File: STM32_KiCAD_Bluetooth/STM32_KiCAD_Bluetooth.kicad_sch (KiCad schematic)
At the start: 9 parts, among them U1 STM32WB55CEU6

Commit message: Schematic
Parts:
- removed C7: 1.0uF, SparkFun-Capacitor:C_0603_1608Metric, symbol SparkFun-Capacitor:1.0uF_0603_16V_10%
- removed C8: 10nF, SparkFun-Capacitor:C_0603_1608Metric, symbol SparkFun-Capacitor:1.0uF_0603_16V_10%
- added C10, C8, C9: 0.1uF, SparkFun-Capacitor:C_0603_1608Metric, symbol SparkFun-Capacitor:0.1uF_0603_25V_20%
- added C11, C7: 4.7uF, SparkFun-Capacitor:C_0603_1608Metric, symbol SparkFun-Capacitor:4.7uF_0603_35V_20%
- added L1: 10nH, Inductor_SMD:L_0603_1608Metric, symbol Device:L
- added L2: 10uH, symbol Device:L
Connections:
- net +3.3V: now also U1.23 (VDDRF), U1.34 (VDDSMPS), U1.8 (VDDA), C10.1, C7.1, C8.1, C9.1
- net GND: now also C10.2, C11.2, C7.2, C8.2, C9.2
- net SMPSFB: now reaches U1.31 (VFBSMPS)
- net SMPSFB: now also C11.1, L2.2
- net SMPSLX: now reaches U1.33 (VLXSMPS)
- net SMPSLX: now also L1.1
- new net SMPSLXL: L1.2, L2.1

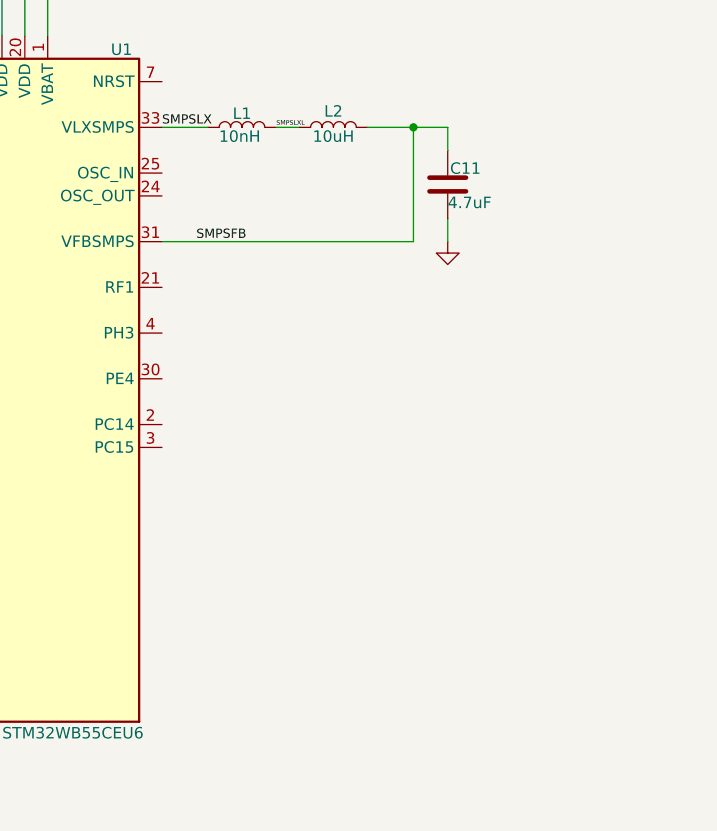
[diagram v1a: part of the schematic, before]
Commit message: Update STM32_KiCAD_Bluetooth.kicad_sch
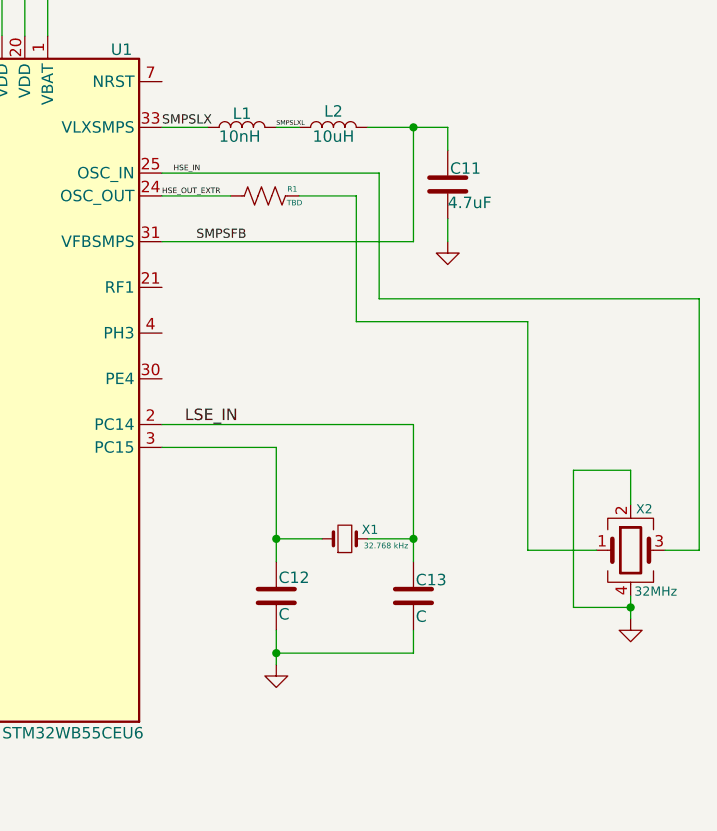
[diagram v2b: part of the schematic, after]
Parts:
- added C12, C13: C, symbol Device:C
- added R1: TBD, SparkFun-Resistor:R_0603_1608Metric, symbol SparkFun-Resistor:330_0603
- added X1: 32.768 kHz, Crystal:Crystal_SMD_2012-2Pin_2.0x1.2mm, symbol SparkFun-Clock:Crystal
- added X2: 32MHz, symbol Device:Crystal_GND24
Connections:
- net GND: now also C12.2, C13.2, X2.2, X2.4
- net LSE_IN: now reaches U1.2 (PC14)
- net LSE_IN: now also C13.1, X1.2
- net HSE_OUT_EXTR: now reaches U1.24 (OSC_OUT)
- net HSE_OUT_EXTR: now also R1.2
- net HSE_IN: now reaches U1.25 (OSC_IN)
- net HSE_IN: now also X2.3
- net at U1.3 (PC15): now also C12.1, X1.1
- new net: R1.1, X2.1

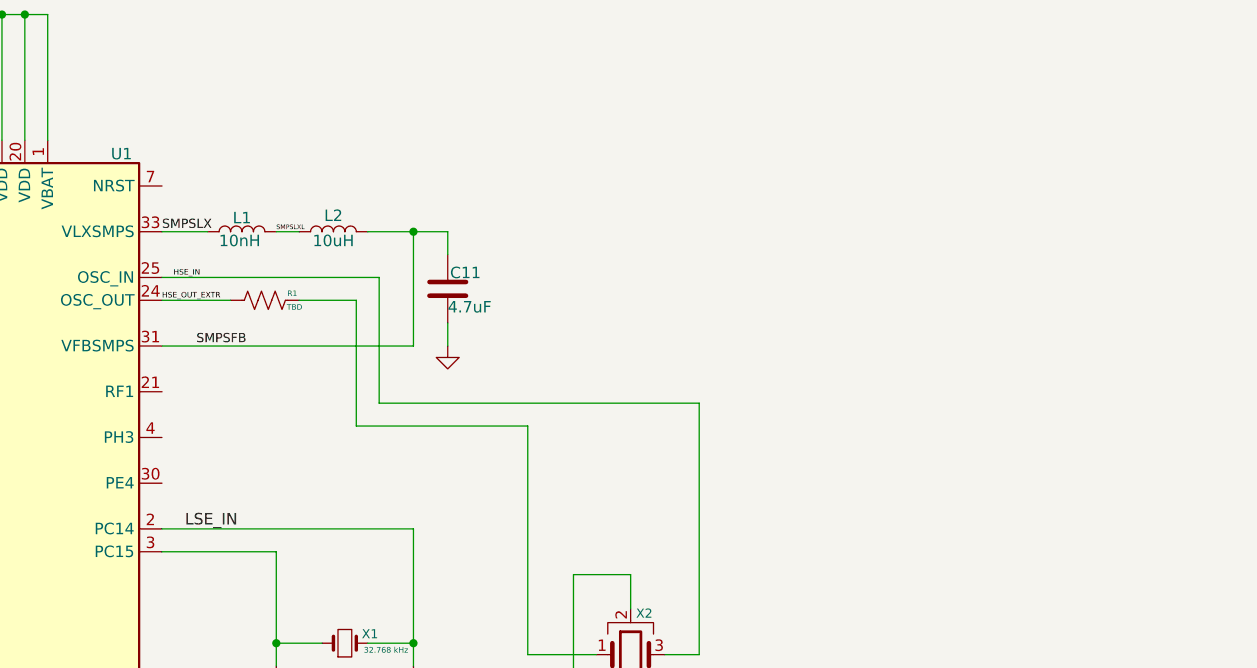
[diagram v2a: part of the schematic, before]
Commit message: Added antenna
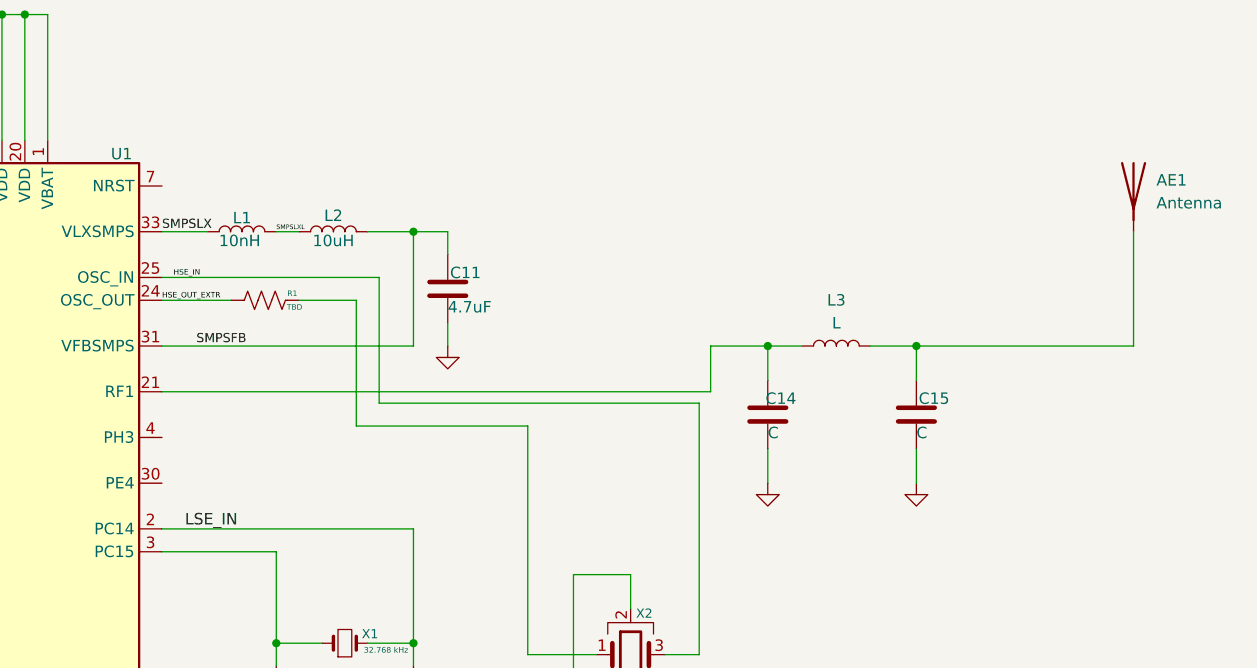
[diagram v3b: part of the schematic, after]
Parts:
- added AE1: Antenna, symbol Device:Antenna
- added C14: C, symbol Device:C
- added C15: C, SparkFun-Capacitor:C_0603_1608Metric, symbol SparkFun-Capacitor:4.7uF_0603_35V_20%
- added L3: L, symbol Device:L
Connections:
- net GND: now also C14.2, C15.2
- net at U1.21 (RF1): now also C14.1, L3.1
- new net: AE1.1 (A), C15.1, L3.2
